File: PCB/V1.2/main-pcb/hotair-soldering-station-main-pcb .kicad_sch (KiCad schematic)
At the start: 96 parts, among them J1 230VAC_IN, J10 T12_power (NS-25 r2,54), J11 LCD_CON2 (JST r.2.0), J12 LCD_CON1 (JST r.2.0), J13 ICP (goldpin r2,54), J14 T12_signal (NS-25 r2,54), J2 FRONT_PANEL (IDC r. 2,54), J3 EARTH_GND, J4 24V_IN (NS-25 r2,54), J5 PSUPPLY (PWZ-02S r.3,96), J6 HOTAIR_FAN (JST r,2,54), J7 HOTAIR_MEAS (JST r.2,5), J8 HOTAIR_HEATER (PWZ-02S r.3,96), J9 WEP (r.2,54), Q1 BC817, Q10 FP3055LP, Q11 BC817, Q2 BC807, Q3 BC817, Q4 Q_PMOS_GDS, Q5 BC817, Q6 BT139-600, Q7 BC817, Q8 FP3055LP, Q9 BC817, U1 MOC3041M, U2 MAX31855KASA, U3 MP1584-Step-Down, U4 AP1117-ADJ, U6 LM358, U7 MAX31855KASA, U8 STM32F103C6Tx

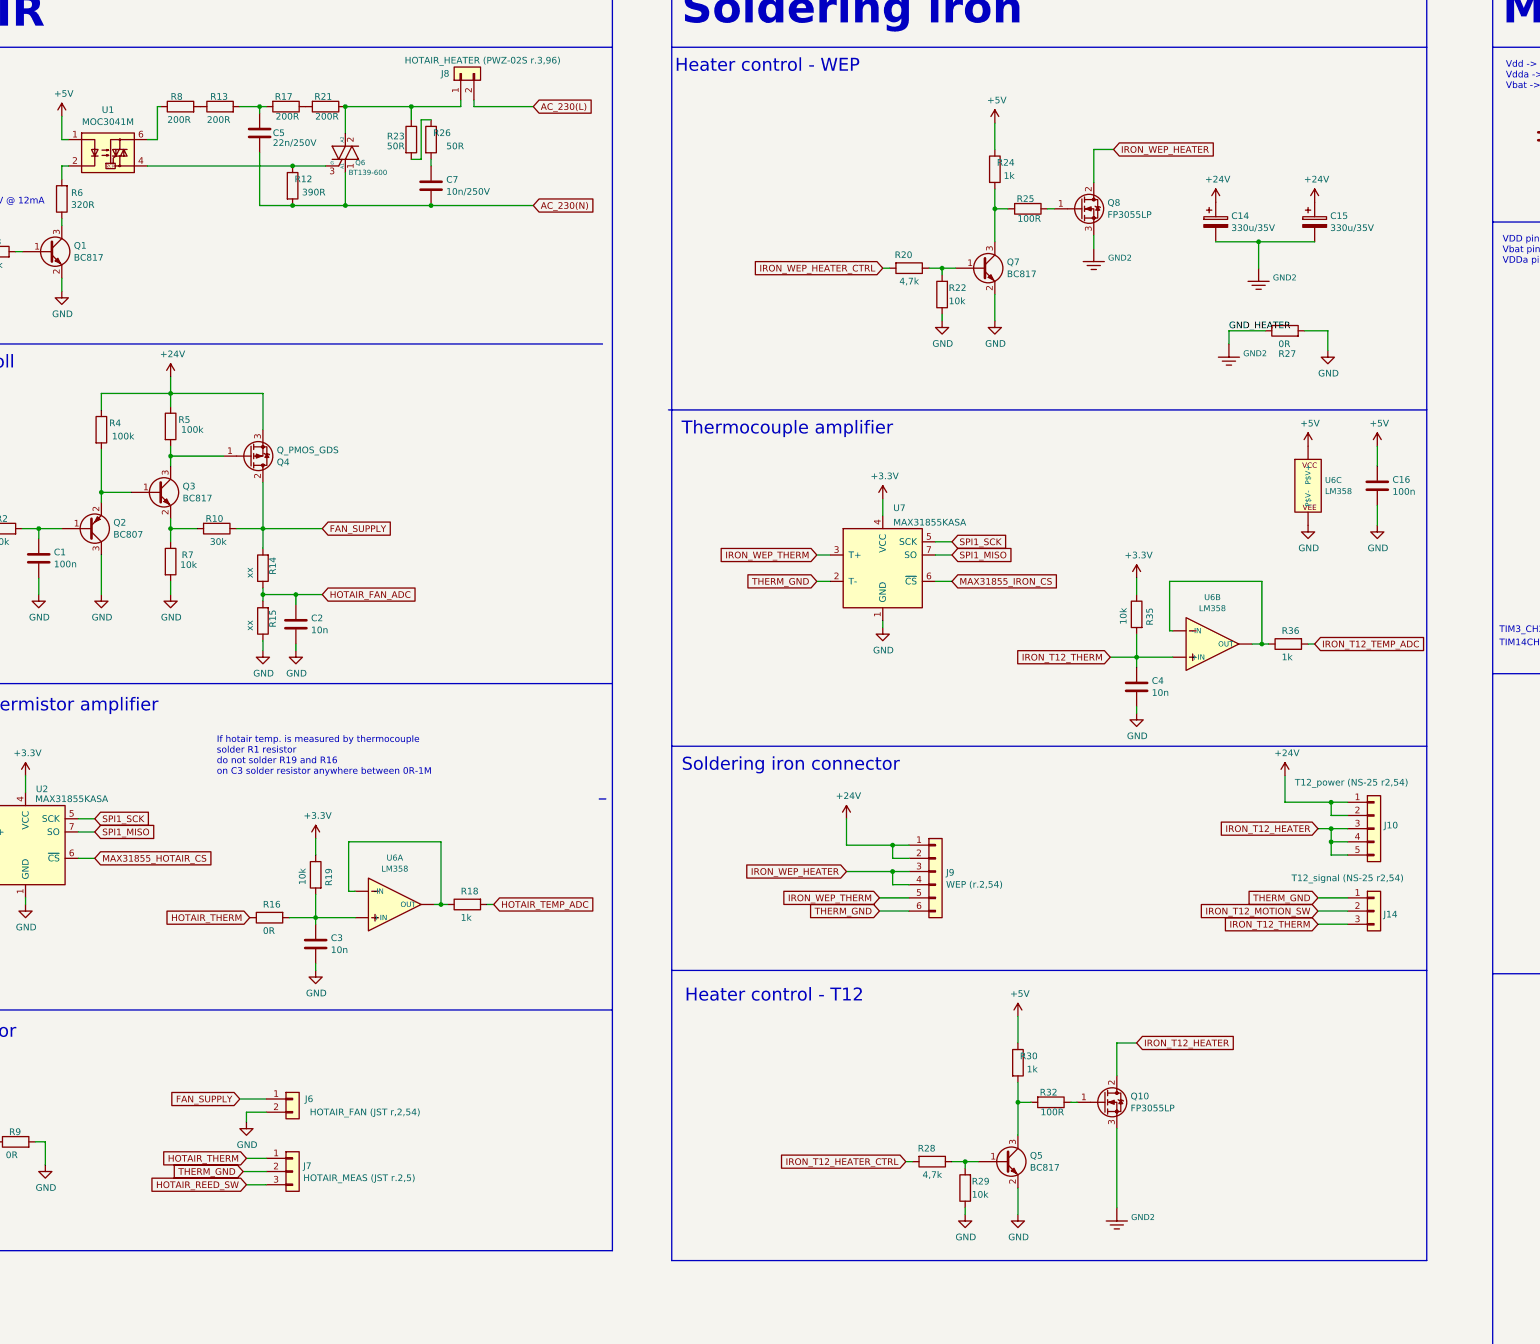
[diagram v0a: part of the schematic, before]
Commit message: T12 and WEP tests done
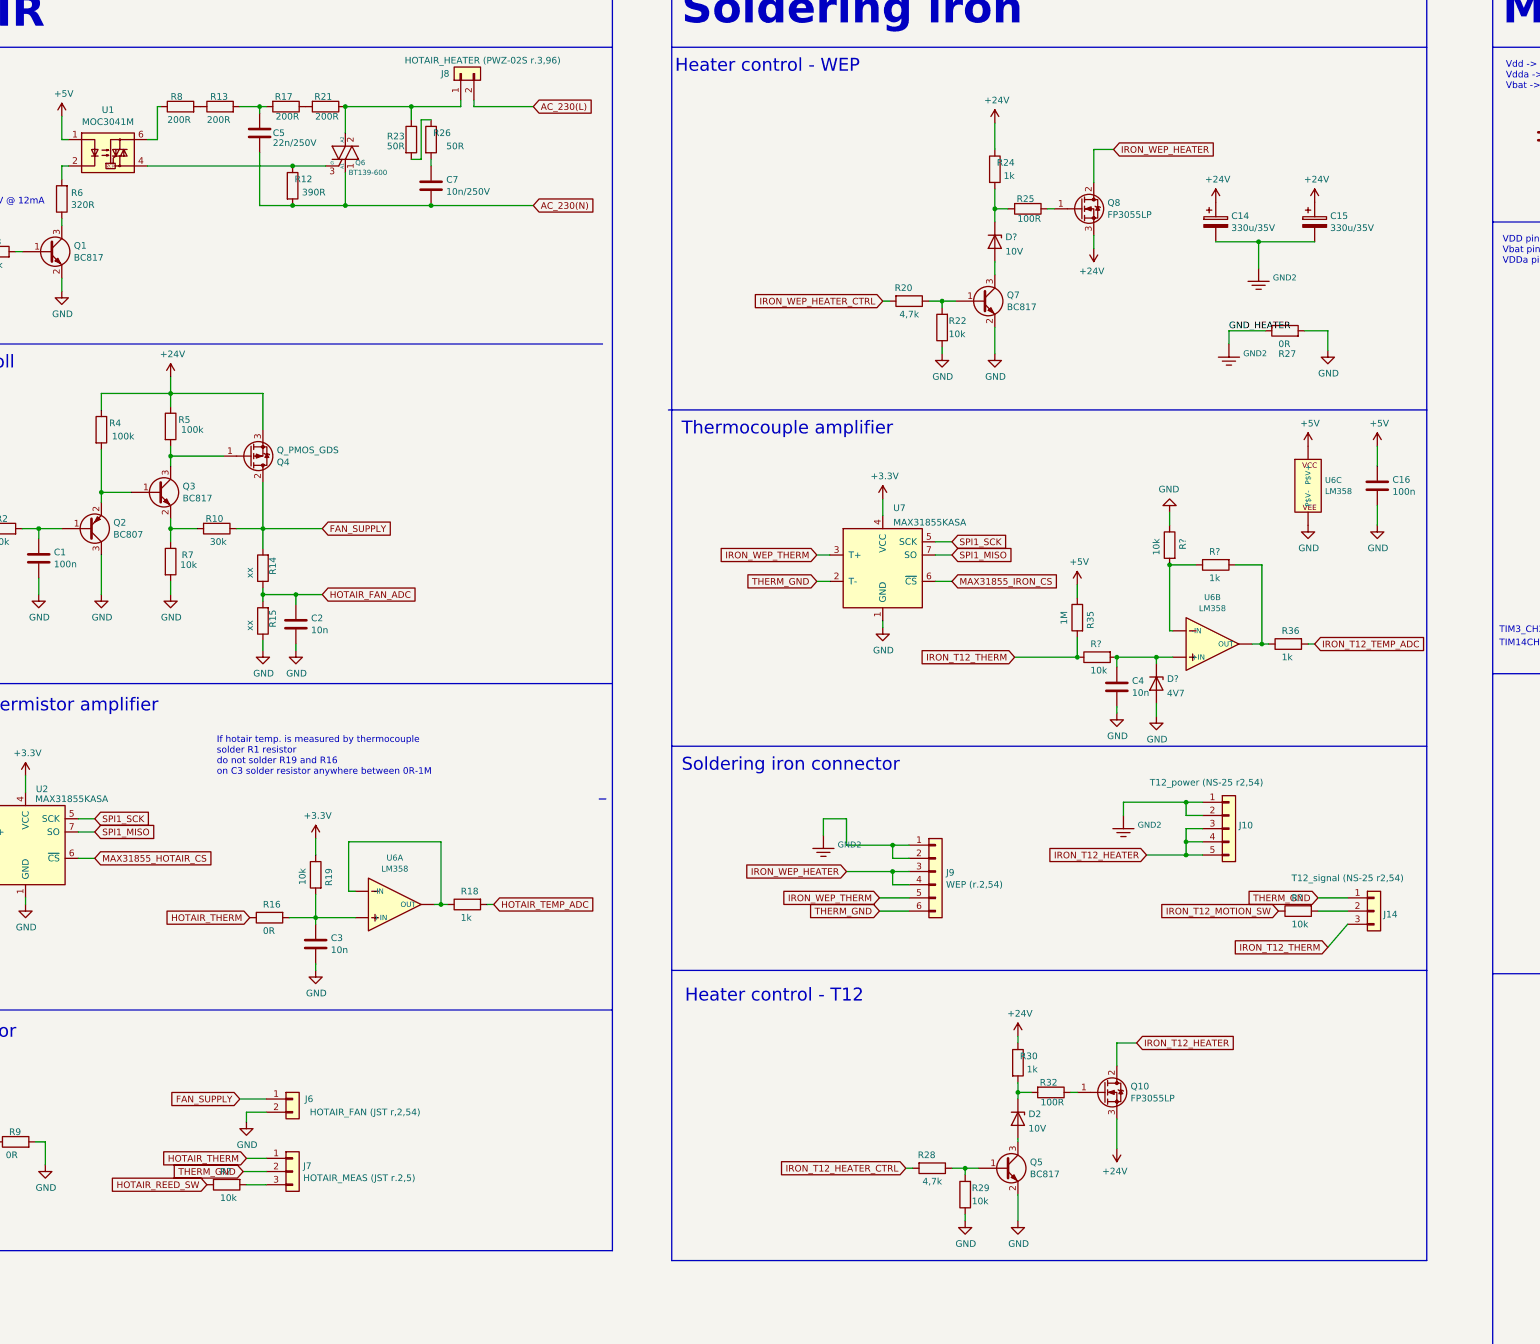
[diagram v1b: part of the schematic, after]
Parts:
- added D2, D?: 10V, Diode_SMD:D_0805_2012Metric, symbol Device:D_Zener
- added D?: 4V7, Diode_SMD:D_0805_2012Metric, symbol Device:D_Zener
- added R? (x4): 10k, Capacitors:0805, symbol Device:R
- added R?: 1k, Capacitors:0805, symbol Device:R
- R35: value 10k -> 1M
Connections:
- net +24V: now also Q10.3 (S), Q8.3 (S), R24.1, R30.1; no longer J10.1 (Pin_1), J10.2 (Pin_2), J9.1 (Pin_1), J9.2 (Pin_2)
- net +3V3: no longer R35.1
- net +5V: now also R35.1; no longer R24.1, R30.1
- net GND: now also D?.2 (A), R?.1
- net GND2: now also J10.1 (Pin_1), J10.2 (Pin_2), J9.1 (Pin_1), J9.2 (Pin_2); no longer Q10.3 (S), Q8.3 (S)
- net HOTAIR_REED_SW: now also R?.1; no longer J7.3 (Pin_3)
- net IRON_T12_MOTION_SW: now also R?.1; no longer J14.2 (Pin_2)
- net IRON_T12_THERM: now also R?.1; no longer C4.1, U6.5 (+IN)
- net at R24.2, R25.2: now also D?.1 (K); no longer Q7.3 (C)
- net at R36.1, U6.7 (OUT): now also R?.2; no longer U6.6 (-IN)
- net at R30.2, R32.2: now also D2.1 (K); no longer Q5.3 (C)
- new net: J7.3 (Pin_3), R?.2
- new net: D?.2 (A), Q7.3 (C)
- new net: D2.2 (A), Q5.3 (C)
- new net: C4.1, D?.1 (K), R?.2, U6.5 (+IN)
- new net: R?.1, R?.2, U6.6 (-IN)
- new net: J14.2 (Pin_2), R?.2
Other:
- moved on the sheet: C4, J10, Q10, Q5, Q7, R20, R22, R28, R29, R32, R35

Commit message: Ideas and documentation of station, schematic V1.2 update
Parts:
- removed C15: 330u/35V, Capacitors_ThroughHole:CP_Radial_D10.0mm_P5.00mm, symbol Device:CP
- removed C3: 10n, Capacitors:0805, symbol Device:C
- removed D?: 4V7, Diode_SMD:D_0805_2012Metric, symbol Device:D_Zener
- removed R16: 0R, Capacitors:0805, symbol Device:R
- removed R18: 1k, Capacitors:0805, symbol Device:R
- removed R19: 10k, Capacitors:0805, symbol Device:R
- removed U7: MAX31855KASA, Package_SO:SOIC-8_3.9x4.9mm_P1.27mm, symbol Sensor_Temperature:MAX31855KASA
- added C?: 10n, Capacitors:0805, symbol Device:C
- added D? (x4): 1N4148, Diodes_SMD:D_MiniMELF, symbol Device:D
- added D? (x2): 3V6, Diode_SMD:D_0805_2012Metric, symbol Device:D_Zener
- added R?: 2k2, Capacitors:0805, symbol Device:R
- added R?: 200k, Capacitors:0805, symbol Device:R
- added R?: 1k, Capacitors:0805, symbol Device:R
- added R?: 10k, Capacitors:0805, symbol Device:R
- added R?: 1M, Capacitors:0805, symbol Device:R
- R14: value xx -> 33k
- R15: value xx -> 2k2
- R36: value 1k -> 2k2
- R?: value 1k -> 200k
- R?: value 10k -> 1k
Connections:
- net +5V: now also R?.1
- net GND: now also C?.2, D?.1 (K), D?.1 (K), D?.2 (A), D?.2 (A), D?.2 (A), D?.2 (A), R?.1
- net HOTAIR_TEMP_ADC: now also D?.1 (K), R?.2
- net HOTAIR_THERM: now also R?.1, R?.2
- net IRON_T12_TEMP_ADC: now also D?.1 (K)
- net at U6.1 (OUT): now also R?.1, R?.2; no longer U6.2 (-IN)
- net at Q8.1 (G), R25.1: now also R24.2
- net at D?.1 (K), R25.2: no longer R24.2
- net at U6.3 (+IN): now also C?.1, D?.1 (K), D?.2 (A), R?.2
- net at C4.1, R?.2, U6.5 (+IN): now also D?.1 (K), D?.2 (A)
- new net: R?.1, R?.2, U6.2 (-IN)
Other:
- note added: "Thermocouple amplifier - T12"
- note removed: "If hotair temp. is measured by thermocouple solder R1 resistor do not solder R19 and R16 on C3 solder resistor anywhere between 0R-1M"
- note removed: "Thermocouple amplifier"
- moved on the sheet: C14, C4, D?, J10, J14, J6, J9, Q7, Q8, R1, R20, R22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

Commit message: Main and front PCB schematic rearrangement.
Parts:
- removed R1: 0R, Capacitors:0805, symbol Device:R
- removed U2: MAX31855KASA, Package_SO:SOIC-8_3.9x4.9mm_P1.27mm, symbol Sensor_Temperature:MAX31855KASA
- added C?: 10n, Capacitors:0805, symbol Device:C
- added R? (x2): 47k, Capacitors:0805, symbol Device:R
- added U?: MAX31855KASA, Package_SO:SOIC-8_3.9x4.9mm_P1.27mm, symbol Sensor_Temperature:MAX31855KASA
- F1: value 3,15A -> 1,5A
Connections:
- net +3V3: now also U?.4 (VCC)
- net GND: now also R?.1, R?.1, U?.1 (GND)
- net MAX31855_IRON_CS: now also U?.6 (~{CS})
- net SPI1_MISO: now also U?.7 (SO)
- net SPI1_SCK: now also U?.5 (SCK)
- net THERM_GND: no longer J9.6 (Pin_6)
- net at Q1.1 (B), R3.2: now also R?.2
- net at Q9.1 (B), R31.1: now also R?.2
- net IRON_WEP_THERM renamed IRON_WEP_THERM+
- net IRON_WEP_THERM+: now also C?.1, U?.3 (T+)
- net MAX31855_HOTAIR_CS: no longer names the net of U8.14 (PA4)
- new net IRON_WEP_THERM-: C?.2, J9.6 (Pin_6), U?.2 (T-)
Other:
- note added: "Heater control"
- note added: "LCD Connectors contrast and backlight circuit"
- note added: "Soldering iron - T12"
- note added: "Soldering iron - WEP"
- note added: "Thermocouple amplifier"
- note removed: "Heater control - T12"
- note removed: "Heater control - WEP"
- note removed: "Soldering iron"
- note removed: "Thermocouple amplifier - T12"
- moved on the sheet: C12, C13, C14, C16, C18, C19, C20, C4, C5, C6, C7, C8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

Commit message: Schematic V1.2: Drawed concept of new mosfet gate driver,  a lot of minor changes
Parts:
- removed D2: 10V, Diode_SMD:D_0805_2012Metric, symbol Device:D_Zener
- removed J14: T12_signal (NS-25 r2,54), Connector:Conn-01x03-N25-W4P, symbol Connector_Generic:Conn_01x03
- removed J3: EARTH_GND, My-Footprints:Screw-Terminal-5.00mm-2pin, symbol Connector:Screw_Terminal_01x02
- removed Q10, Q8: FP3055LP, Package_TO_SOT_THT:TO-220-3_Vertical, symbol Device:Q_NMOS_GDS
- removed Q5: BC817, Package_TO_SOT_SMD:SOT-23, symbol Transistor_BJT:BC817
- removed R28: 4,7k, Capacitors:0805, symbol Device:R
- removed R29: 10k, Capacitors:0805, symbol Device:R
- removed R30: 1k, Capacitors:0805, symbol Device:R
- removed R32: 100R, Capacitors:0805, symbol Device:R
- added C?: 100n, Capacitors:0603, symbol Device:C
- added C? (x2): 10n, Capacitors:0805, symbol Device:C
- added D?: 12V, Diode_SMD:D_0805_2012Metric, symbol Device:D_Zener
- added D?: (no value), symbol Device:D_Schottky
- added D?: SR310, Diode_SMD:D_SMA, symbol Device:D_Schottky
- added J?: (no value), symbol Connector:Screw_Terminal_01x03
- added Q? (x3): BC817, Package_TO_SOT_SMD:SOT-23, symbol Transistor_BJT:BC817
- added Q?: (no value), symbol Transistor_BJT:BC807
- added Q?: (no value), symbol Device:Q_PMOS_DGS
- added Q?: BC807, Package_TO_SOT_SMD:SOT-23, symbol Transistor_BJT:BC807
- added Q?: RFP15P05, Package_TO_SOT_THT:TO-220-3_Vertical, symbol Device:Q_PMOS_DGS
- added R? (x2): (no value), symbol Device:R
- added R?: 1k5, Capacitors:0805, symbol Device:R
- added R?: 100R, Capacitors:0805, symbol Device:R
- added R?: (no value), Capacitors:0805, symbol Device:R
- added R? (x4): 10k, Capacitors:0805, symbol Device:R
- added R?: 430R, Capacitors:0805, symbol Device:R
- added R?: 100k, Capacitors:0805, symbol Device:R
- added R?: 2k2, Capacitors:0805, symbol Device:R
- D?: value 10V -> (none); footprint Diode_SMD:D_0805_2012Metric -> (none)
- Q4: value Q_PMOS_GDS -> (none); footprint Power_Integrations:TO-220 -> (none)
- R20: value 4,7k -> (none); footprint Capacitors:0805 -> (none)
- R24: value 1k -> (none); footprint Capacitors:0805 -> (none)
- R38, R40: value xx -> (none); footprint Capacitors:0805 -> (none)
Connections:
- net IRON_T12_THERM is gone; now on net IRON_T12_THERM_HEATER: R35.2, R?.1
- net +24V: now also D?.2 (A), D?.1 (K), D?.1 (K), D?.1 (K), Q?.3 (C), Q?.3 (C), Q?.3 (S), Q?.3 (S), R?.1, R?.2, R?.2
- net +3V3: now also R?.2, R?.2
- net +5V: now also R?.2, R?.2
- net GND: now also C?.2, Q?.3 (C), Q?.3 (C), R?.1, R?.1, R?.1; no longer Q7.2 (E)
- net GND2: now also J10.3 (Pin_3); no longer J10.1 (Pin_1)
- net IRON_T12_HEATER_CTRL: now also C?.1, R?.2
- net IRON_WEP_HEATER: now also D?.2 (A), Q?.1 (D)
- net IRON_WEP_HEATER_CTRL: now also C?.1
- net RST: now also C?.1, R?.1
- net UART_DBG_TX: now also R?.1
- net at J7.3 (Pin_3), R?.2: now also R?.1
- net at R24.2: now also R25.2, Q?.2 (G); no longer R25.1
- net at Q7.1 (B), R20.1, R22.2: now also C?.2
- net at Q7.3 (C): now also D?.1 (K), Q?.1 (B), Q?.1 (B), R?.1; no longer D?.2 (A)
- net at J1.1 (Pin_1): now also J?.1 (Pin_1), J?.2 (Pin_2), J?.3 (Pin_3)
- net at R?.2: now also J10.1 (Pin_1), R?.1
- net IRON_T12_HEATER renamed IRON_T12_THERM_HEATER
- net IRON_T12_THERM_HEATER: now also D?.2 (A), Q?.1 (D); no longer J10.3 (Pin_3)
- new net: Q7.2 (E), R?.2
- new net: Q?.2 (E), Q?.2 (E), R25.1
- new net: D?.2 (A), Q?.1 (B), Q?.1 (B), Q?.3 (C), R?.1
- new net: Q?.2 (E), Q?.2 (E), R?.1
- new net: Q?.2 (G), R?.2, R?.2
- new net: C?.2, Q?.1 (B), R?.1, R?.2
- new net: Q?.2 (E), R?.2
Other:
- note added: "Do zrobienia: - ptrzetwornica sprawdzić czy pinout ok - dobrać bezpiecznik polimerowy - konektor LCD bez plątaniny kable na prosto - sprawdzić wzmaniacz operacyjny model - sprawdzić czy zamiast max mozna by dac opamp"
- moved on the sheet: D?, J13, J6, J7, Q7, R20, R22, R24, R25, R9, R?

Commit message: Schematic and PCB update
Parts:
- removed F2: Polyfuse, Fuse:Fuse_Bourns_MF-RG500, symbol Device:Polyfuse
- D1, D10, D2, D8: renamed from D?; footprint Diodes_SMD:D_MiniMELF -> Diode_SMD:D_MiniMELF
- D11, D3: renamed from D?; footprint Diode_SMD:D_0805_2012Metric -> Diode_SMD:D_MiniMELF
- D4: renamed from D?; value (none) -> 12V; footprint (none) -> Diode_SMD:D_0805_2012Metric
- D6: renamed from D?; value (none) -> SR310; footprint (none) -> Diode_SMD:D_SMA
- J3: renamed from J?; value (none) -> EARTH_GND; footprint (none) -> My-Footprints:Screw-Terminal-5.00mm-3pin
- Q10: renamed from Q?; value (none) -> RFP15P05; footprint (none) -> My-Footprints:TO-220-3_V_Thick_Pads
- Q15: renamed from Q?; footprint Package_TO_SOT_THT:TO-220-3_Vertical -> My-Footprints:TO-220-3_V_Thick_Pads
- Q4: value (none) -> RFP15P05; footprint (none) -> My-Footprints:TO-220-3_V_Thick_Pads
- Q6: footprint My-Footprints:TO-220-3_Vertical -> My-Footprints:TO-220-3_V_Wide_Legs
- Q8: renamed from Q?; value (none) -> BC807; footprint (none) -> Package_TO_SOT_SMD:SOT-23
- R20: value (none) -> 2k2; footprint (none) -> Capacitors:0805
- R24: value (none) -> 100k; footprint (none) -> Capacitors:0805
- R38: value (none) -> 24k; footprint (none) -> Capacitors:0805
- R40: value (none) -> 2k; footprint (none) -> Capacitors:0805
- R41: renamed from R?; value (none) -> 1k5
- R42: renamed from R?; value (none) -> 430R; footprint (none) -> Capacitors:0805
- R55: renamed from R?; value (none) -> 10k; footprint (none) -> Capacitors:0805
- gave numbers to parts that had none: 33
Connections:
- net +24V: now also J4.3 (Pin_3), J4.4 (Pin_4)
